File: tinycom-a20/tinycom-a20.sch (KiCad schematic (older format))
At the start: 36 parts, among them P1 CONN_02X08, P2 CONN_02X08, U1 ALLWINNERA10/TFBGA441, U2 H5TQG63BFR/FBGA96, U3 H27UBG8T2A/TSOP48, Y1 Crystal_Small, Y2 Crystal_Small

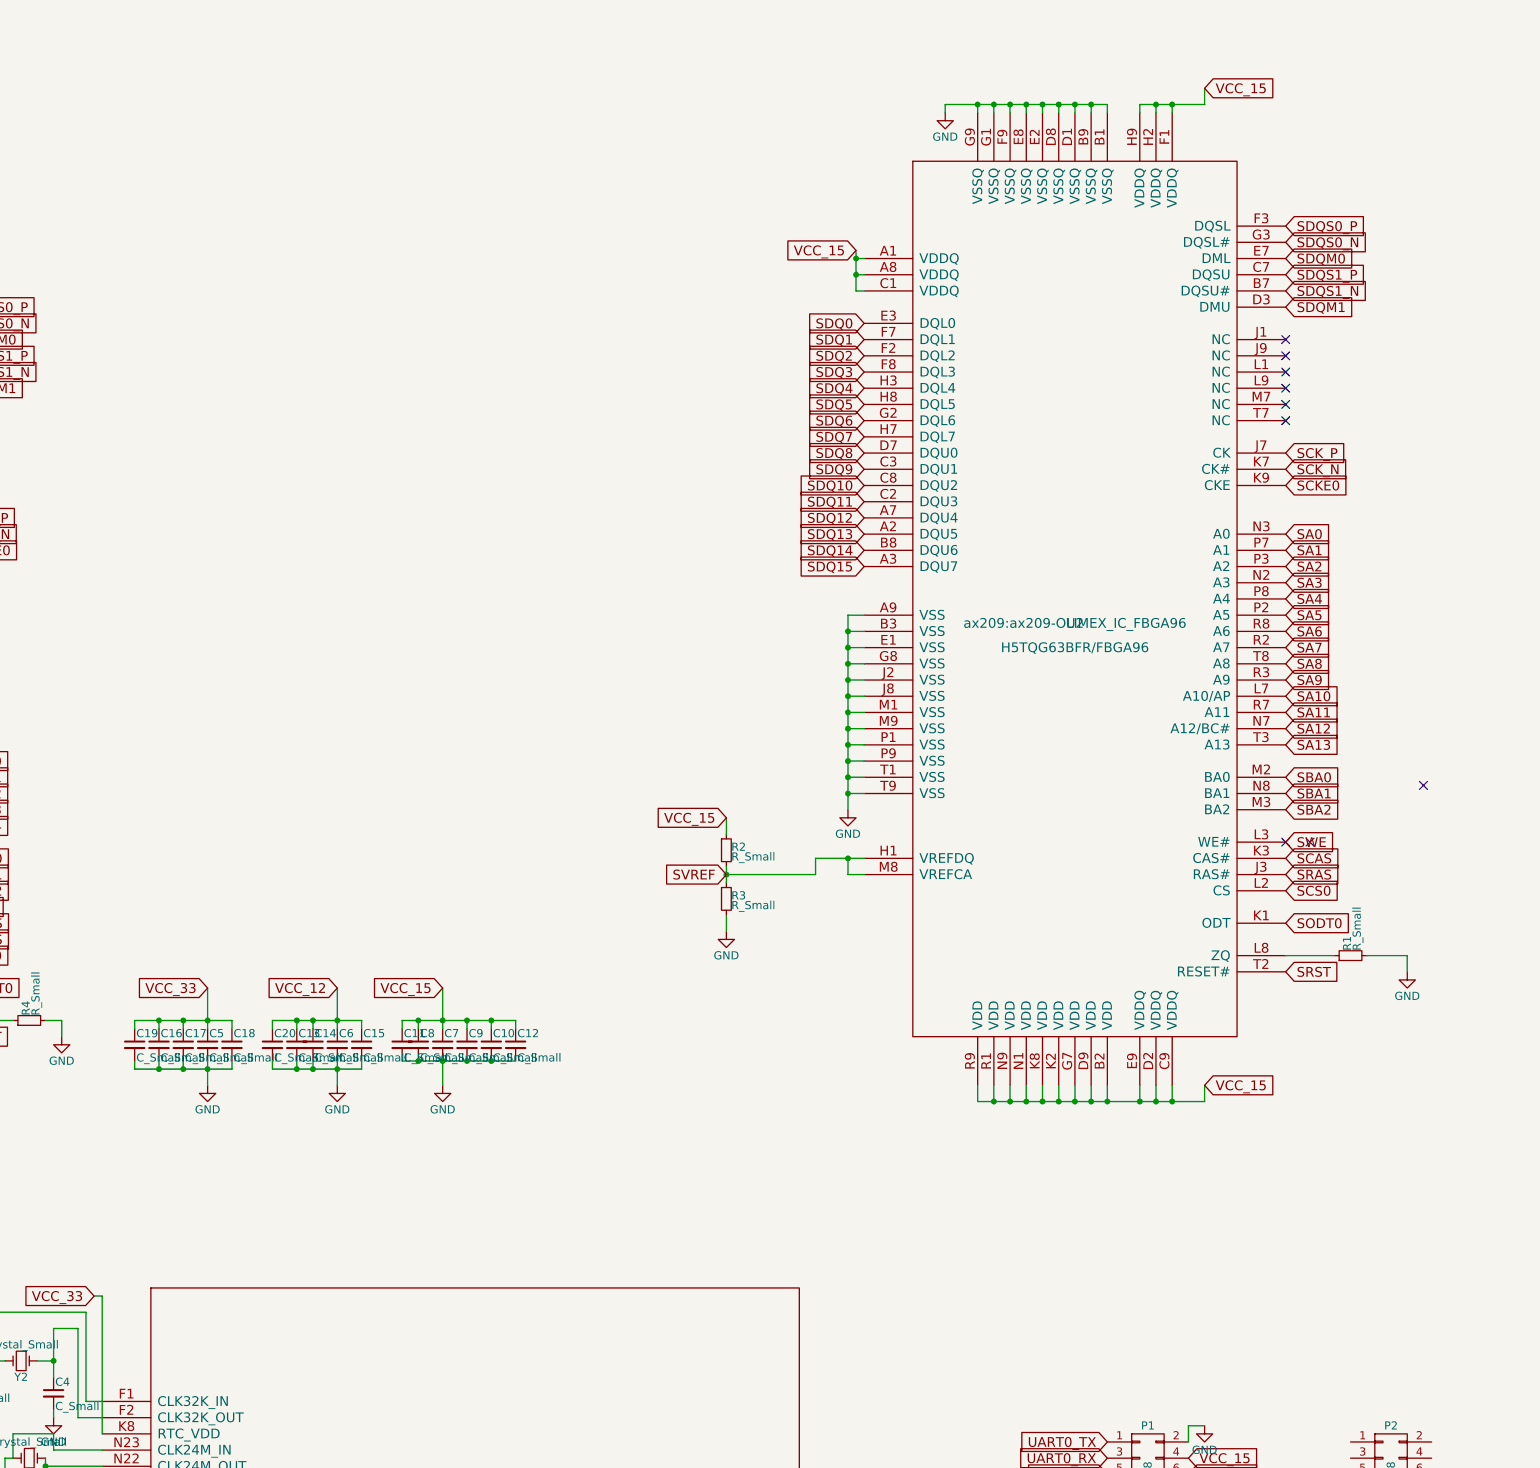
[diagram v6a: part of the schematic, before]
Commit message: add 2nd ddr
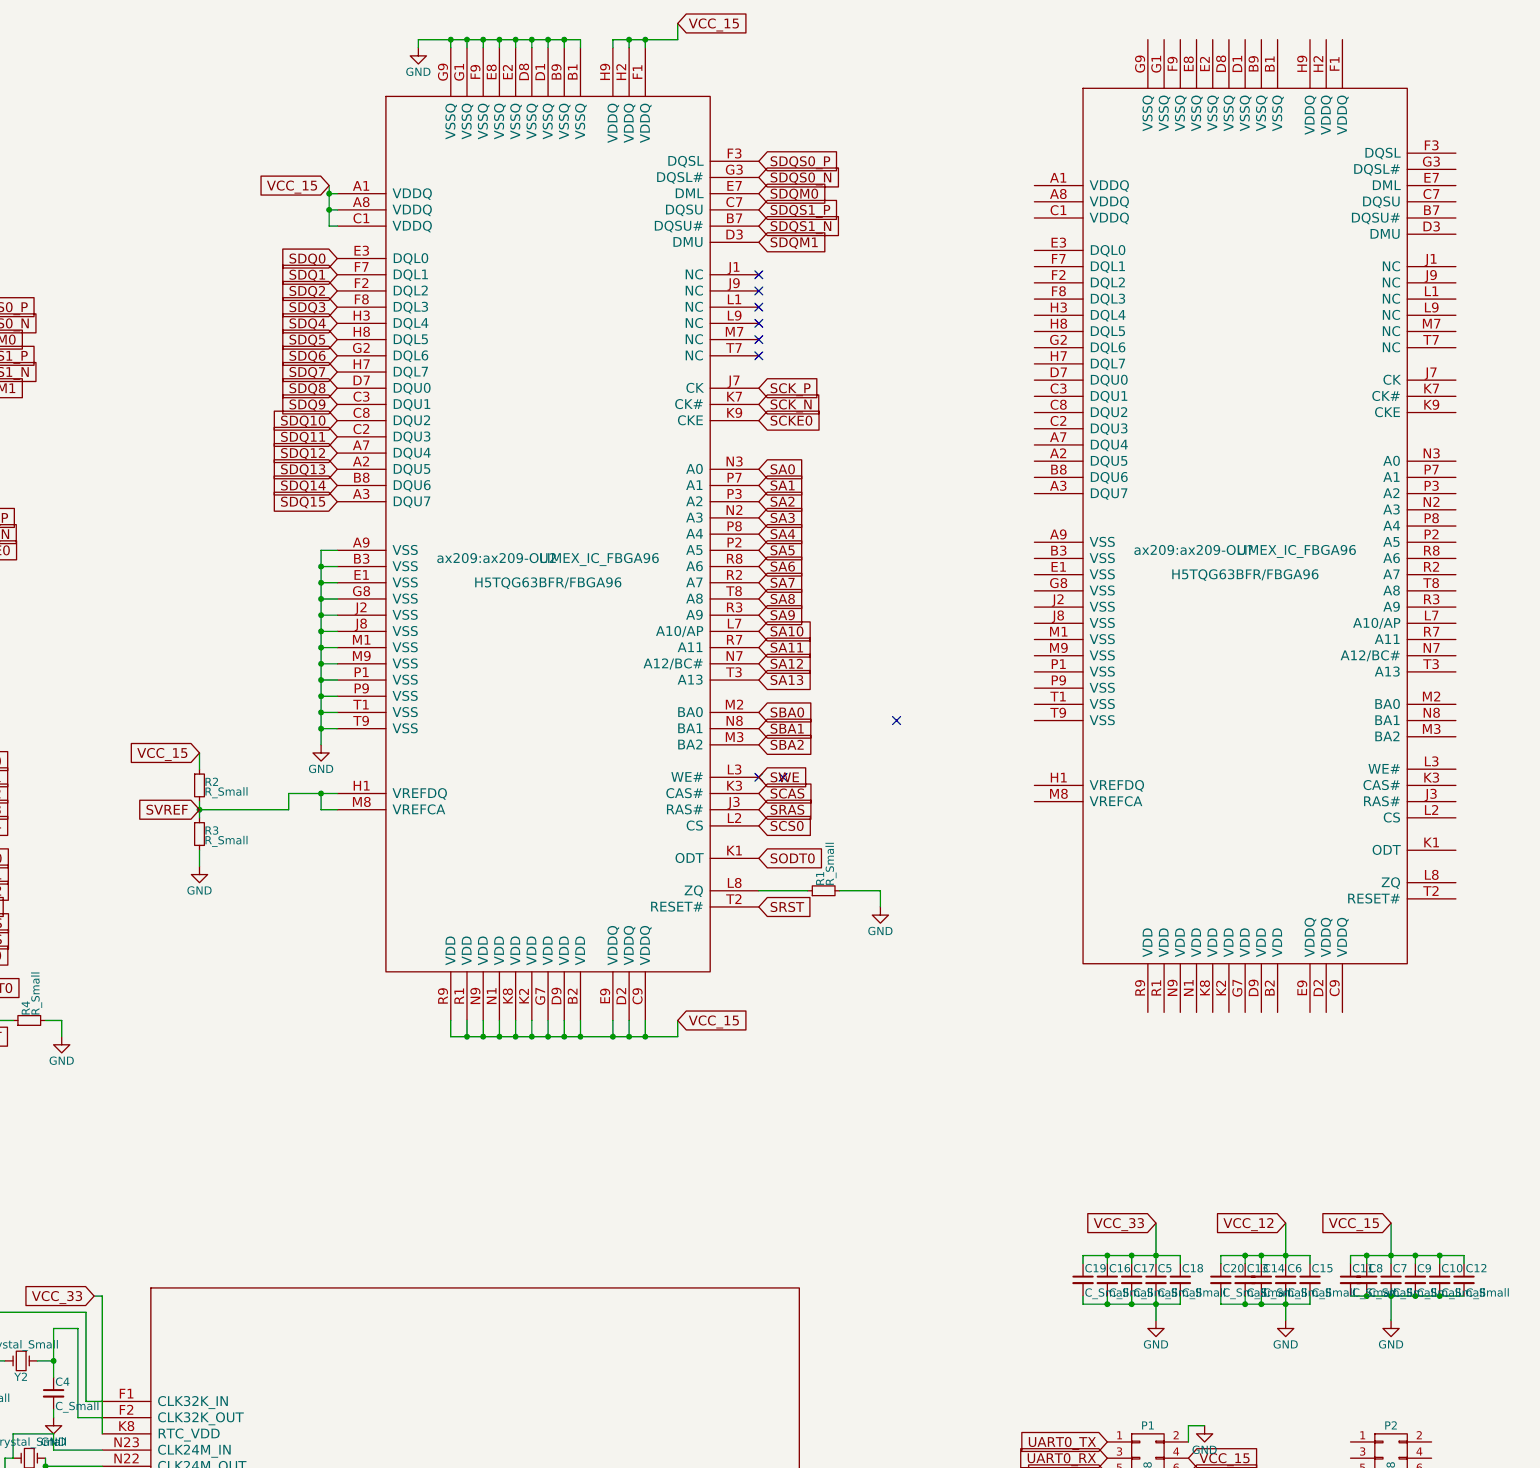
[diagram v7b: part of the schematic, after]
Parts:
- added U?: H5TQG63BFR/FBGA96, ax209:ax209-OLIMEX_IC_FBGA96, symbol H5TQG63BFR/FBGA96
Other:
- moved on the sheet: C10, C11, C12, C13, C14, C15, C16, C17, C18, C19, C20, C5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

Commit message: delete tracks
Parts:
- added R10: R_Small, Resistors_SMD:R_0603, symbol R_Small
- gave numbers to parts that had none: 1
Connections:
- net GND: now also U4.A9 (VSS), U4.B1 (VSSQ), U4.B3 (VSS), U4.B9 (VSSQ), U4.D1 (VSSQ), U4.D8 (VSSQ), U4.E1 (VSS), U4.E2 (VSSQ), U4.E8 (VSSQ), U4.F9 (VSSQ), U4.G1 (VSSQ), U4.G8 (VSS), U4.G9 (VSSQ), U4.J2 (VSS), U4.J8 (VSS), U4.M1 (VSS), U4.M9 (VSS), U4.P1 (VSS), U4.P9 (VSS), U4.T1 (VSS), U4.T9 (VSS), R10.2
- net SA0: now also U4.N3 (A0)
- net SA1: now also U4.P7 (A1)
- net SA10: now also U4.L7 (A10/AP)
- net SA11: now also U4.R7 (A11)
- net SA12: now also U4.N7 (A12/BC#)
- net SA13: now also U4.T3 (A13)
- net SA2: now also U4.P3 (A2)
- net SA3: now also U4.N2 (A3)
- net SA4: now also U4.P8 (A4)
- net SA5: now also U4.P2 (A5)
- net SA6: now also U4.R8 (A6)
- net SA7: now also U4.R2 (A7)
- net SA8: now also U4.T8 (A8)
- net SA9: now also U4.R3 (A9)
- net SBA0: now also U4.M2 (BA0)
- net SBA1: now also U4.N8 (BA1)
- net SBA2: now also U4.M3 (BA2)
- net SCAS: now also U4.K3 (CAS#)
- net SCKE0: now also U4.K9 (CKE)
- net SCK_N: now also U4.K7 (CK#)
- net SCK_P: now also U4.J7 (CK)
- net SCS0: now also U4.L2 (CS)
- net SODT0: now also U4.K1 (ODT)
- net SRAS: now also U4.J3 (RAS#)
- net SRST: now also U4.T2 (RESET#)
- net SVREF: now also U4.H1 (VREFDQ), U4.M8 (VREFCA)
- net SWE: now also U4.L3 (WE#)
- net VCC_15: now also U4.A1 (VDDQ), U4.A8 (VDDQ), U4.B2 (VDD), U4.C1 (VDDQ), U4.C9 (VDDQ), U4.D2 (VDDQ), U4.D9 (VDD), U4.E9 (VDDQ), U4.F1 (VDDQ), U4.G7 (VDD), U4.H2 (VDDQ), U4.H9 (VDDQ), U4.K2 (VDD), U4.K8 (VDD), U4.N1 (VDD), U4.N9 (VDD), U4.R1 (VDD), U4.R9 (VDD)
- net SDQM3: now reaches U1.G1 (SDQM3)
- net SDQM3: now also U4.D3 (DMU)
- net SDQ30: now reaches U1.G2 (SDQ30)
- net SDQ30: now also U4.B8 (DQU6)
- net SDQ25: now reaches U1.H1 (SDQ25)
- net SDQ25: now also U4.C3 (DQU1)
- net SDQ27: now reaches U1.H2 (SDQ27)
- net SDQ27: now also U4.C2 (DQU3)
- net SDQ28: now reaches U1.J1 (SDQ28)
- net SDQ28: now also U4.A7 (DQU4)
- net SDQS3_N: now reaches U1.J2 (SDQS3#)
- net SDQS3_N: now also U4.B7 (DQSU#)
- net SDQS3_P: now reaches U1.K1 (SDQS3)
- net SDQS3_P: now also U4.C7 (DQSU)
- net SDQ31: now reaches U1.K2 (SDQ31)
- net SDQ31: now also U4.A3 (DQU7)
- net SDQ24: now reaches U1.L1 (SDQ24)
- net SDQ24: now also U4.D7 (DQU0)
- net SDQ26: now reaches U1.L2 (SDQ26)
- net SDQ26: now also U4.C8 (DQU2)
- net SDQ29: now reaches U1.M1 (SDQ29)
- net SDQ29: now also U4.A2 (DQU5)
- net SDQ23: now reaches U1.M2 (SDQ23)
- net SDQ23: now also U4.H7 (DQL7)
- net SDQ16: now reaches U1.N1 (SDQ16)
- net SDQ16: now also U4.E3 (DQL0)
- net SDQ18: now reaches U1.N2 (SDQ18)
- net SDQ18: now also U4.F2 (DQL2)
- net SDQ21: now reaches U1.P1 (SDQ21)
- net SDQ21: now also U4.H8 (DQL5)
- net SDQS2_N: now reaches U1.P2 (SDQS2#)
- net SDQS2_N: now also U4.G3 (DQSL#)
- net SDQS2_P: now reaches U1.R1 (SDQS2)
- net SDQS2_P: now also U4.F3 (DQSL)
- net SDQM2: now reaches U1.R2 (SDQM2)
- net SDQM2: now also U4.E7 (DML)
- net SDQ22: now reaches U1.T1 (SDQ22)
- net SDQ22: now also U4.G2 (DQL6)
- net SDQ17: now reaches U1.T2 (SDQ17)
- net SDQ17: now also U4.F7 (DQL1)
- net SDQ19: now reaches U1.U1 (SDQ19)
- net SDQ19: now also U4.F8 (DQL3)
- net SDQ20: now reaches U1.U2 (SDQ20)
- net SDQ20: now also U4.H3 (DQL4)
- net at U4.L8 (ZQ): now also R10.1
- no-connect marks 258 -> 239
